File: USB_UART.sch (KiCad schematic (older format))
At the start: 7 parts

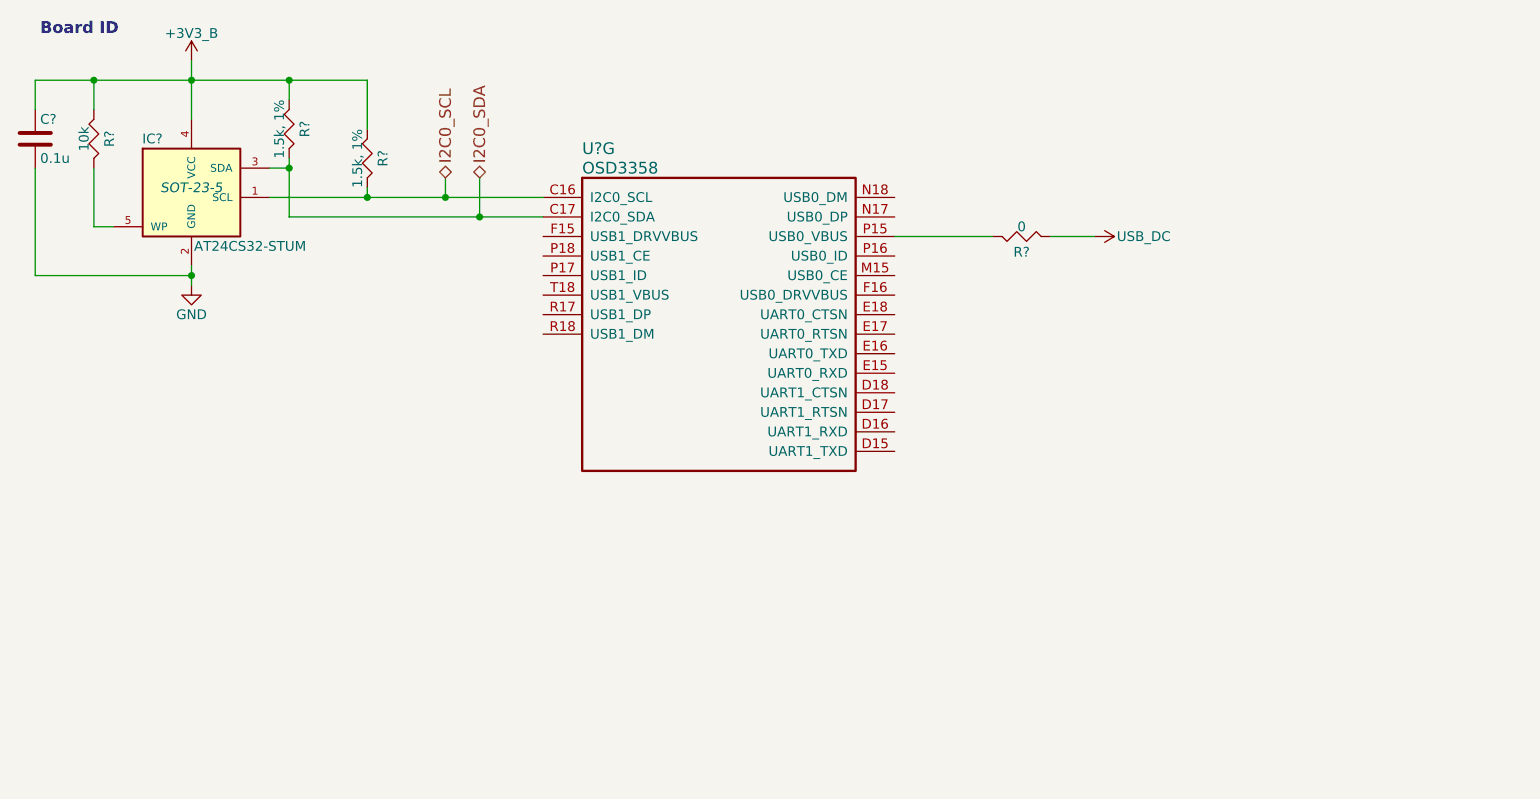
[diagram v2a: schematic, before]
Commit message: Added USB Host and Device
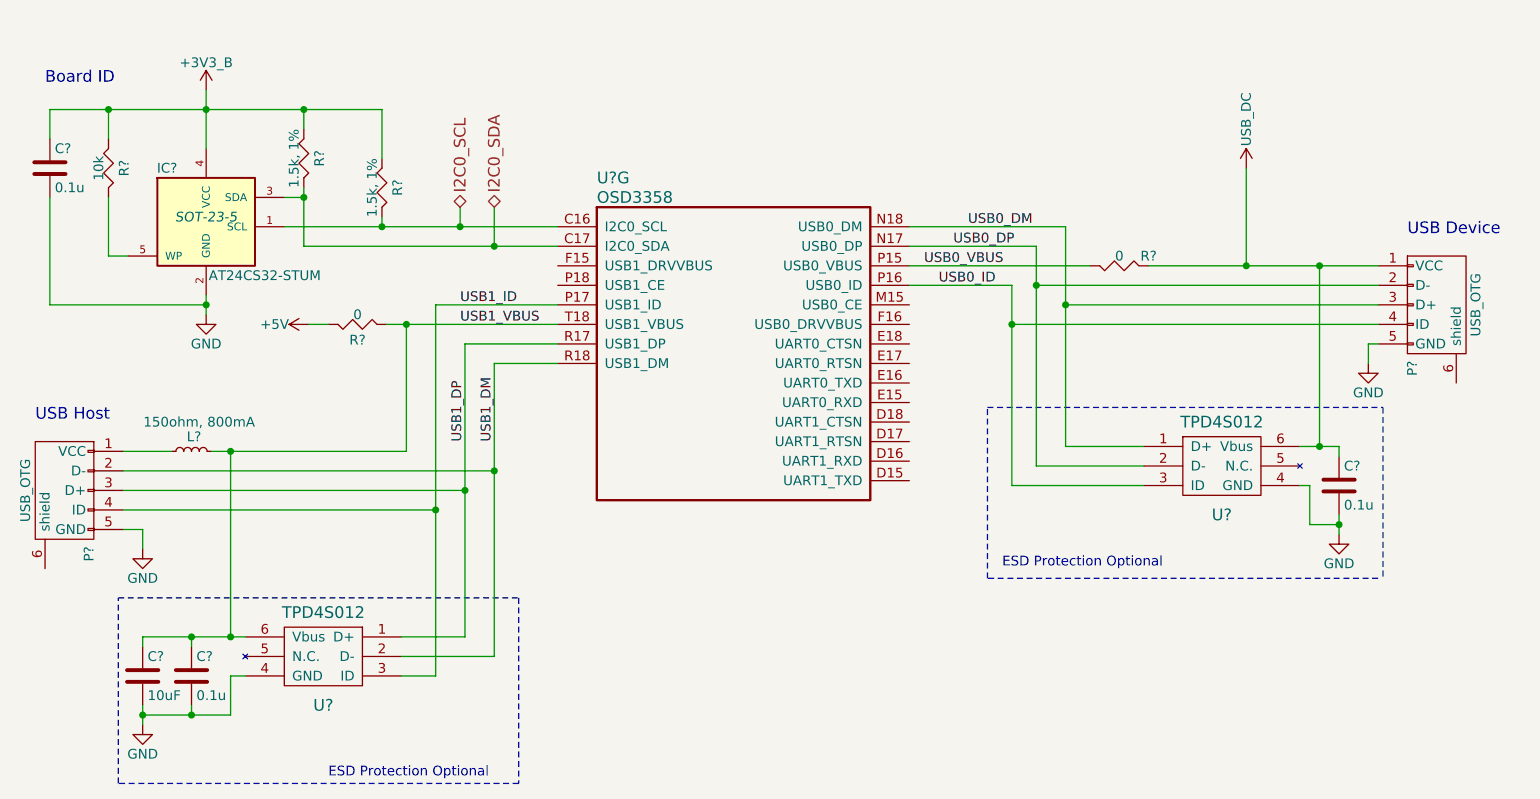
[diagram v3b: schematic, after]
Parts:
- added C? (x2): 0.1u, symbol C
- added C?: 10uF, symbol C
- added L?: 150ohm, 800mA, symbol L_Small
- added P? (x2): USB_OTG, symbol USB_OTG
- added R?: 0, symbol R
- added U? (x2): TPD4S012, symbol TPD4S012
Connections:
- net GND: now also C?.2, C?.2, C?.2, P?.5 (GND), P?.5 (GND), U?.4 (GND), U?.4 (GND)
- net USB_DC: now also C?.1, P?.1 (VCC), U?.6 (Vbus)
- net USB0_DP: now reaches U?.N17 (USB0_DP)
- net USB0_DP: now also P?.2 (D-), U?.2 (D-)
- net USB0_DM: now reaches U?.N18 (USB0_DM)
- net USB0_DM: now also P?.3 (D+), U?.1 (D+)
- net USB0_VBUS: now reaches R?.2, U?.P15 (USB0_VBUS)
- net USB0_ID: now reaches U?.P16 (USB0_ID)
- net USB0_ID: now also P?.4 (ID), U?.3 (ID)
- net USB1_ID: now reaches U?.P17 (USB1_ID)
- net USB1_ID: now also P?.4 (ID), U?.3 (ID)
- net USB1_DP: now reaches U?.R17 (USB1_DP)
- net USB1_DP: now also P?.3 (D+), U?.1 (D+)
- net USB1_DM: now reaches U?.R18 (USB1_DM)
- net USB1_DM: now also P?.2 (D-), U?.2 (D-)
- net USB1_VBUS: now reaches U?.T18 (USB1_VBUS)
- net USB1_VBUS: now also C?.1, C?.1, L?.2, R?.1, U?.6 (Vbus)
- new net: L?.1, P?.1 (VCC)
- new net +5V: R?.2
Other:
- note added: "ESD Protection Optional"
- note added: "USB Device"
- note added: "USB Host"
- moved on the sheet: C?, IC?, R?, U?G

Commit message: Added Sysboot configuration, user LEDs, updated README
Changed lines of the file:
@@
 $Descr A4 11693 8268
 encoding utf-8
-Sheet 2 5
+Sheet 2 6
 Title "IBBB"
 Date "2016-05-15"
@@
 	2850 1950 2950 1950
 Wire Wire Line
-	2950 1900 2950 1950
-Wire Wire Line
-	2950 1950 2950 2200
-Wire Wire Line
-	2850 2100 3350 2100
-Wire Wire Line
-	3350 2100 3750 2100
-Wire Wire Line
-	3750 2100 4250 2100
+	2950 1900 2950 2200
+Wire Wire Line
+	2850 2100 4250 2100
 Wire Wire Line
 	3350 2100 3350 2050
 Connection ~ 3350 2100
 Wire Wire Line
-	2950 2200 3925 2200
-Wire Wire Line
-	3925 2200 4250 2200
+	2950 2200 4250 2200
 Connection ~ 2950 1950
 Wire Wire Line
-	2450 1400 2450 1500
-Wire Wire Line
-	2450 1500 2450 1700
-Wire Wire Line
-	1650 1500 1950 1500
-Wire Wire Line
-	1950 1500 2450 1500
-Wire Wire Line
-	2450 1500 2950 1500
-Wire Wire Line
-	2950 1500 3350 1500
+	2450 1400 2450 1700
+Wire Wire Line
+	1650 1500 3350 1500
 Wire Wire Line
 	2950 1500 2950 1600
@@
 $EndComp
 Wire Wire Line
-	2450 2450 2450 2500
-Wire Wire Line
-	2450 2500 2450 2550
+	2450 2450 2450 2550
 $Comp
 L R R?
@@
 $EndComp
 Wire Wire Line
-	8050 3225 8150 3225
-Wire Wire Line
-	8150 3225 8250 3225
+	8050 3225 8250 3225
 Wire Wire Line
 	8250 3225 8250 3275
@@
 	8100 3625 8250 3625
 Wire Wire Line
-	8250 3575 8250 3625
-Wire Wire Line
-	8250 3625 8250 3675
+	8250 3575 8250 3675
 Connection ~ 8250 3625
 $Comp
@@
 	8400 2700 8400 2800
 Wire Wire Line
-	7275 2300 7775 2300
-Wire Wire Line
-	7775 2300 8150 2300
-Wire Wire Line
-	8150 2300 8450 2300
+	7275 2300 8450 2300
 Wire Wire Line
 	8150 3225 8150 2300
@@
 	6050 2400 6575 2400
 Wire Wire Line
-	6575 2400 6575 2600
-Wire Wire Line
-	6575 2600 6575 3425
+	6575 2400 6575 3425
 Wire Wire Line
 	6575 3425 7250 3425
@@
 	6050 2200 6700 2200
 Wire Wire Line
-	6700 2200 6700 2400
-Wire Wire Line
-	6700 2400 6700 3325
+	6700 2200 6700 3325
 Wire Wire Line
 	6700 3325 7250 3325
@@
 	6050 2100 6850 2100
 Wire Wire Line
-	6850 2100 6850 2500
-Wire Wire Line
-	6850 2500 6850 3225
+	6850 2100 6850 3225
 Wire Wire Line
 	6850 3225 7250 3225
@@
 	2025 3250 2275 3250
 Wire Wire Line
-	2475 3250 2575 3250
-Wire Wire Line
-	2575 3250 3475 3250
+	2475 3250 3475 3250
 Wire Wire Line
 	3475 3250 3475 2600
 Wire Wire Line
-	3375 2600 3475 2600
-Wire Wire Line
-	3475 2600 4250 2600
+	3375 2600 4250 2600
 $Comp
 L R R?
@@
 	2025 3350 3925 3350
 Wire Wire Line
-	3925 2800 3925 3350
-Wire Wire Line
-	3925 3350 3925 4300
+	3925 2800 3925 4300
 Wire Wire Line
 	3925 2800 4250 2800
@@
 	2025 3450 3775 3450
 Wire Wire Line
-	3775 2700 3775 3450
-Wire Wire Line
-	3775 3450 3775 4200
+	3775 2700 3775 4200
 Wire Wire Line
 	3775 2700 4250 2700
@@
 	4250 2500 3625 2500
 Wire Wire Line
-	3625 2500 3625 3550
-Wire Wire Line
-	3625 3550 3625 4400
+	3625 2500 3625 4400
 Wire Wire Line
 	3625 3550 2025 3550
@@
 $EndComp
 Wire Wire Line
-	2125 4200 2375 4200
-Wire Wire Line
-	2375 4200 2575 4200
-Wire Wire Line
-	2575 4200 2650 4200
+	2125 4200 2650 4200
 Wire Wire Line
 	2575 4200 2575 3250
@@
 $EndComp
 Wire Wire Line
-	2125 4550 2125 4600
-Wire Wire Line
-	2125 4600 2125 4650
+	2125 4550 2125 4650
 Wire Wire Line
 	2375 4550 2375 4600
 Wire Wire Line
-	2125 4600 2375 4600
-Wire Wire Line
-	2375 4600 2575 4600
+	2125 4600 2575 4600
 Connection ~ 2125 4600
 Wire Wire Line
